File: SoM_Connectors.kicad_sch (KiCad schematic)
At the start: 5 parts, among them SW1 SW_DIP_x02

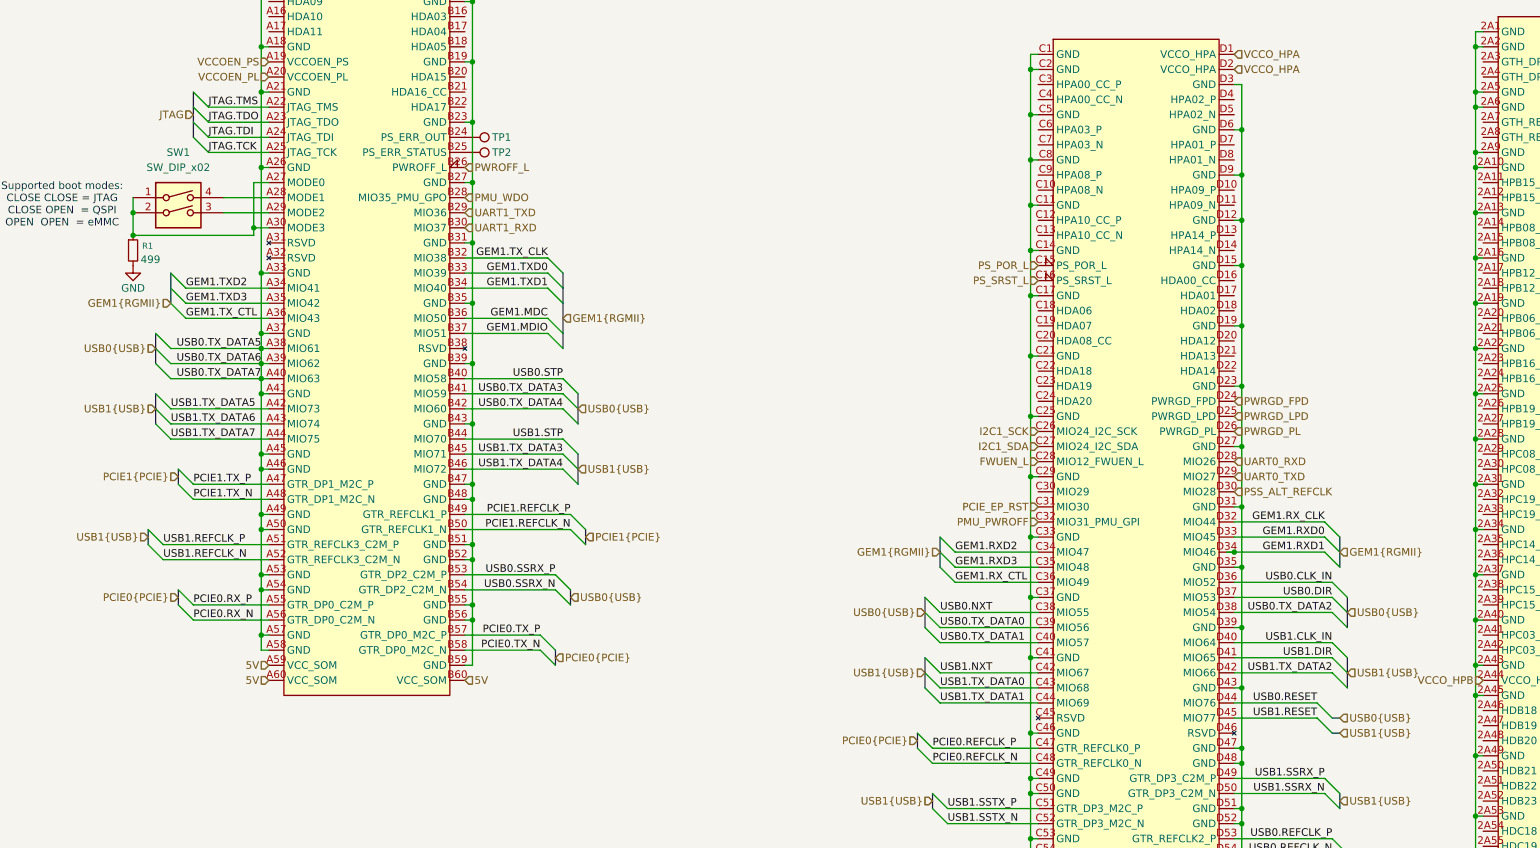
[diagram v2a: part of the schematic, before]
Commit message: MIO changes USB resets from 76/77 to shared 29 GEM1 MDIO moved from 50/51 to 76/77 I2C0 enabled on 50/51
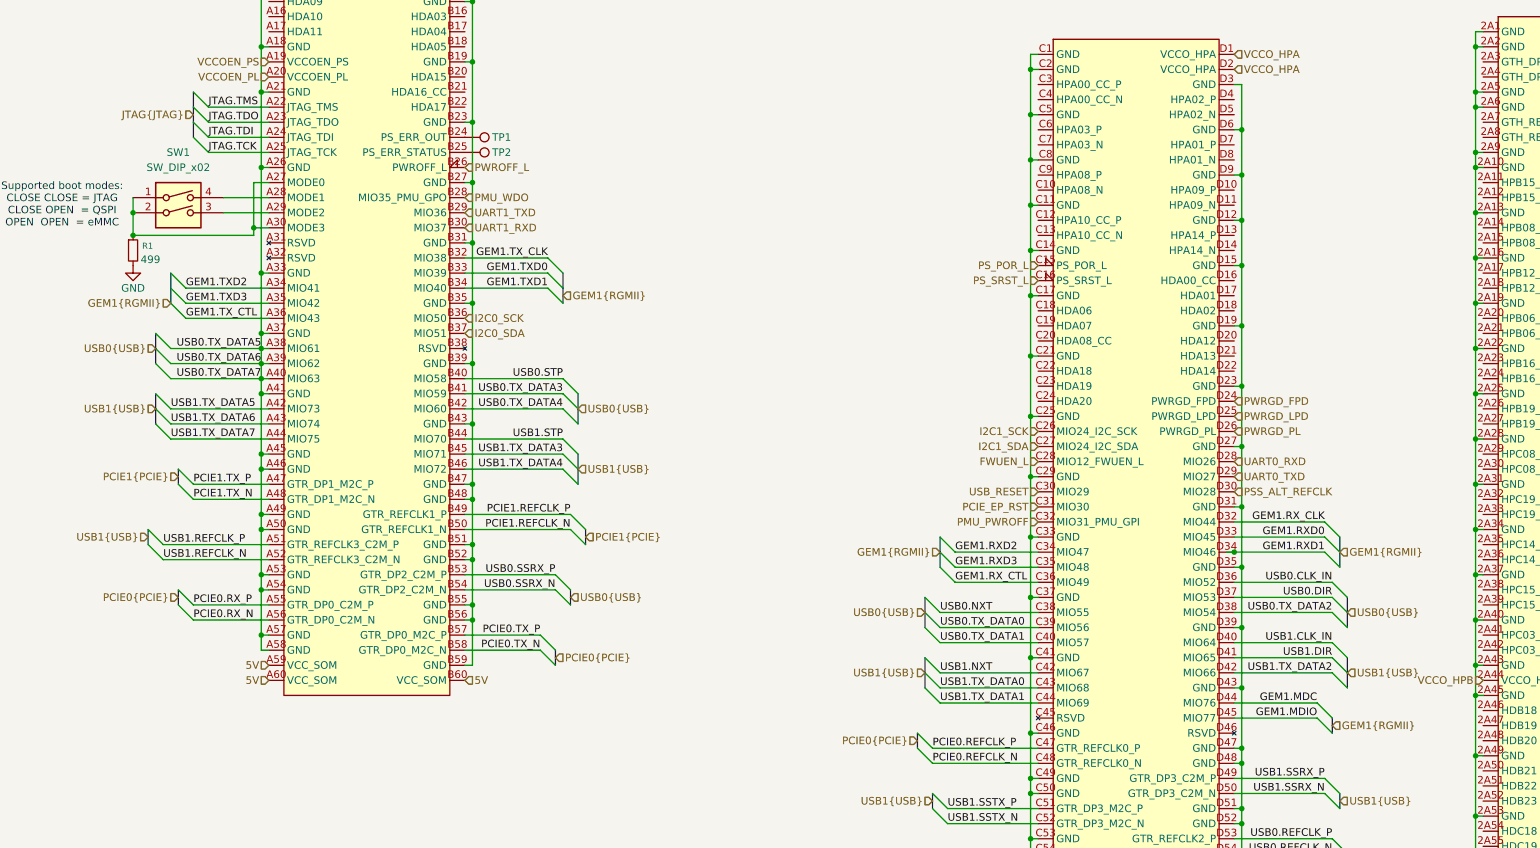
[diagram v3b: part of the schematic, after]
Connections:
- net USB0.RESET is gone; now on net GEM1.MDC: U1.D44 (MIO76)
- net USB1.RESET is gone; now on net GEM1.MDIO: U1.D45 (MIO77)
- net GEM1.MDC: no longer U1.B36 (MIO50)
- net GEM1.MDIO: no longer U1.B37 (MIO51)
- net USB_RESET: now reaches U1.C30 (MIO29)
- new net I2C0_SCK: U1.B36 (MIO50)
- new net I2C0_SDA: U1.B37 (MIO51)
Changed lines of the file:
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@@
 	)
 	(bus_entry
-		(at 105.41 185.42)
+		(at 236.22 196.85)
 		(size 2.54 2.54)
 		(stroke
@@
 	)
 	(bus_entry
-		(at 172.72 194.31)
-		(size -2.54 -2.54)
+		(at 105.41 185.42)
+		(size 2.54 2.54)
 		(stroke
 			(width 0)
@@
 	)
 	(bus_entry
-		(at 49.53 93.98)
+		(at 172.72 194.31)
 		(size -2.54 -2.54)
 		(stroke
@@
 	)
 	(bus_entry
-		(at 236.22 194.31)
-		(size 2.54 2.54)
+		(at 49.53 93.98)
+		(size -2.54 -2.54)
 		(stroke
 			(width 0)
@@
 	)
 	(bus_entry
-		(at 106.68 132.08)
-		(size 2.54 2.54)
-		(stroke
-			(width 0)
-			(type default)
-		)
-	)
-	(bus_entry
 		(at 107.95 172.72)
 		(size 2.54 2.54)
@@
 	)
 	(bus_entry
-		(at 106.68 129.54)
-		(size 2.54 2.54)
-		(stroke
-			(width 0)
-			(type default)
-		)
-	)
-	(bus_entry
-		(at 236.22 196.85)
+		(at 236.22 194.31)
 		(size 2.54 2.54)
 		(stroke
@@
 		)
 	)
-	(wire
-		(pts
-			(xy 106.68 132.08) (xy 92.71 132.08)
-		)
-		(stroke
-			(width 0)
-			(type default)
-		)
-	)
 	(bus
 		(pts
@@
 		)
 	)
+	(bus
+		(pts
+			(xy 238.76 196.85) (xy 238.76 199.39)
+		)
+		(stroke
+			(width 0)
+			(type default)
+		)
+	)
 	(wire
 		(pts
@@
 		)
 	)
-	(wire
-		(pts
-			(xy 106.68 129.54) (xy 92.71 129.54)
-		)
-		(stroke
-			(width 0)
-			(type default)
-		)
-	)
 	(bus
 		(pts
@@
 	(wire
 		(pts
-			(xy 236.22 194.31) (xy 222.25 194.31)
-		)
-		(stroke
-			(width 0)
-			(type default)
-		)
-	)
-	(wire
-		(pts
 			(xy 297.18 99.06) (xy 298.45 99.06)
 		)
@@
 	(wire
 		(pts
+			(xy 236.22 196.85) (xy 222.25 196.85)
+		)
+		(stroke
+			(width 0)
+			(type default)
+		)
+	)
+	(wire
+		(pts
 			(xy 262.89 142.24) (xy 264.16 142.24)
 		)
@@
 		)
 	)
-	(bus
-		(pts
-			(xy 109.22 132.08) (xy 109.22 134.62)
-		)
-		(stroke
-			(width 0)
-			(type default)
-		)
-	)
 	(wire
 		(pts
@@
 		)
 	)
-	(bus
-		(pts
-			(xy 109.22 127) (xy 109.22 132.08)
-		)
-		(stroke
-			(width 0)
-			(type default)
-		)
-	)
 	(wire
 		(pts
@@
 	(wire
 		(pts
-			(xy 236.22 196.85) (xy 222.25 196.85)
-		)
-		(stroke
-			(width 0)
-			(type default)
-		)
-	)
-	(wire
-		(pts
 			(xy 325.12 101.6) (xy 325.12 104.14)
 		)
@@
 		)
 	)
-	(bus
-		(pts
-			(xy 238.76 199.39) (xy 240.03 199.39)
-		)
-		(stroke
-			(width 0)
-			(type default)
-		)
-	)
 	(wire
 		(pts
@@
 		)
 	)
+	(wire
+		(pts
+			(xy 236.22 194.31) (xy 222.25 194.31)
+		)
+		(stroke
+			(width 0)
+			(type default)
+		)
+	)
 	(bus
 		(pts
@@
 		)
 	)
-	(bus
-		(pts
-			(xy 238.76 196.85) (xy 240.03 196.85)
-		)
-		(stroke
-			(width 0)
-			(type default)
-		)
-	)
 	(wire
 		(pts
@@
 		)
 	)
-	(label "USB1.SSRX_N"
-		(at 237.49 209.55 180)
+	(label "GEM1.MDC"
+		(at 236.22 194.31 180)
 		(effects
 			(font
@@
 		)
 	)
-	(label "USB1.RESET"
-		(at 236.22 196.85 180)
+	(label "USB1.SSRX_N"
+		(at 237.49 209.55 180)
 		(effects
 			(font
@@
 		)
 	)
-	(label "USB0.RESET"
-		(at 236.22 194.31 180)
-		(effects
-			(font
-				(size 1.27 1.27)
-			)
-			(justify right bottom)
-		)
-	)
 	(label "USB0.TX_DATA7"
 		(at 58.42 139.7 180)
@@
 		)
 	)
+	(label "GEM1.MDIO"
+		(at 236.22 196.85 180)
+		(effects
+			(font
+				(size 1.27 1.27)
+			)
+			(justify right bottom)
+		)
+	)
 	(label "USB0.REFCLK_N"
 		(at 238.76 219.71 180)
@@
 		)
 	)
-	(label "GEM1.MDC"
-		(at 106.68 129.54 180)
-		(effects
-			(font
-				(size 1.27 1.27)
-			)
-			(justify right bottom)
-		)
-	)
 	(label "GEM1.TXD2"
 		(at 45.72 124.46 0)
@@
 		)
 	)
-	(label "GEM1.MDIO"
-		(at 106.68 132.08 180)
-		(effects
-			(font
-				(size 1.27 1.27)
-			)
-			(justify right bottom)
-		)
-	)
 	(label "JTAG.TMS"
 		(at 49.53 93.98 0)
@@
 		)
 	)
-	(hierarchical_label "USB0{USB}"
-		(shape input)
-		(at 240.03 196.85 0)
-		(effects
-			(font
-				(size 1.27 1.27)
-			)
-			(justify left)
-		)
-	)
 	(hierarchical_label "USB1{USB}"
 		(shape input)
@@
 	(hierarchical_label "GEM1{RGMII}"
 		(shape input)
-		(at 109.22 129.54 0)
+		(at 109.22 125.73 0)
 		(effects
 			(font
@@
 		)
 	)
-	(hierarchical_label "JTAG"
+	(hierarchical_label "JTAG{JTAG}"
 		(shape input)
 		(at 46.99 95.25 180)
@@
 		)
 	)
+	(hierarchical_label "USB_RESET"
+		(shape input)
+		(at 189.23 158.75 180)
+		(effects
+			(font
+				(size 1.27 1.27)
+			)
+			(justify right)
+		)
+	)
 	(hierarchical_label "USB0{USB}"
 		(shape input)
@@
 		)
 	)
+	(hierarchical_label "GEM1{RGMII}"
+		(shape input)
+		(at 238.76 198.12 0)
+		(effects
+			(font
+				(size 1.27 1.27)
+			)
+			(justify left)
+		)
+	)
 	(hierarchical_label "VCCO_HPA"
 		(shape input)
@@
 		)
 	)
-	(hierarchical_label "PMU_PWROFF"
+	(hierarchical_label "I2C0_SCK"
 		(shape input)
-		(at 189.23 163.83 180)
+		(at 92.71 129.54 0)
 		(effects
 			(font
 				(size 1.27 1.27)
 			)
-			(justify right)
+			(justify left)
 		)
 	)
-	(hierarchical_label "5V"
+	(hierarchical_label "I2C0_SDA"
 		(shape input)
-		(at 92.71 190.5 0)
+		(at 92.71 132.08 0)
 		(effects
 			(font
@@
 		)
 	)
-	(hierarchical_label "USB1{USB}"
+	(hierarchical_label "PMU_PWROFF"
 		(shape input)
-		(at 241.3 189.23 0)
+		(at 189.23 163.83 180)
+		(effects
+			(font
+				(size 1.27 1.27)
+			)
+			(justify right)
+		)
+	)
+	(hierarchical_label "5V"
+		(shape input)
+		(at 92.71 190.5 0)
 		(effects
 			(font
@@
 	(hierarchical_label "USB1{USB}"
 		(shape input)
-		(at 240.03 199.39 0)
+		(at 241.3 189.23 0)
 		(effects
 			(font

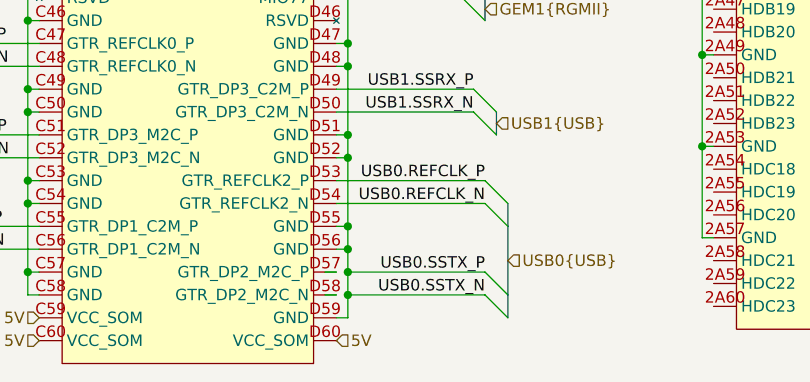
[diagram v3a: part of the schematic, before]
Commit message: fixed USB0.SSTX connections fixed JTAG bus label adjust hier pins in top schematic fixed USB4750 footprint shield pins names
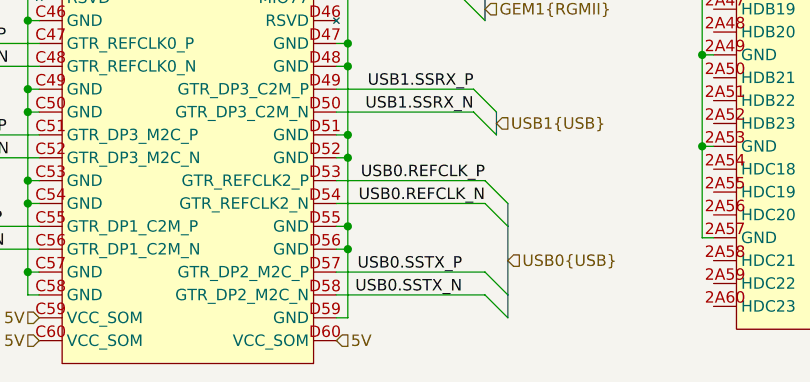
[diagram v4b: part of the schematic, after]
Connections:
- net USB0.SSTX_N: now also U1.D58 (GTR_DP2_M2C_N); no longer U1.D12 (GND), U1.D15 (GND), U1.D19 (GND), U1.D23 (GND), U1.D27 (GND), U1.D3 (GND), U1.D31 (GND), U1.D35 (GND), U1.D39 (GND), U1.D43 (GND), U1.D47 (GND), U1.D48 (GND), U1.D51 (GND), U1.D52 (GND), U1.D55 (GND), U1.D56 (GND), U1.D59 (GND), U1.D6 (GND), U1.D9 (GND)
- net USB0.SSTX_P: now reaches U1.D57 (GTR_DP2_M2C_P)
- new net: U1.D12 (GND), U1.D15 (GND), U1.D19 (GND), U1.D23 (GND), U1.D27 (GND), U1.D3 (GND), U1.D31 (GND), U1.D35 (GND), U1.D39 (GND), U1.D43 (GND), U1.D47 (GND), U1.D48 (GND), U1.D51 (GND), U1.D52 (GND), U1.D55 (GND), U1.D56 (GND), U1.D59 (GND), U1.D6 (GND), U1.D9 (GND)
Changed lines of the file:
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@@
 	)
 	(junction
-		(at 223.52 229.87)
-		(diameter 0)
-		(color 0 0 0 0)
-	)
-	(junction
 		(at 360.68 152.4)
 		(diameter 0)
@@
 	)
 	(junction
-		(at 223.52 227.33)
-		(diameter 0)
-		(color 0 0 0 0)
-	)
-	(junction
 		(at 360.68 167.64)
 		(diameter 0)
@@
 	(wire
 		(pts
-			(xy 223.52 224.79) (xy 223.52 227.33)
-		)
-		(stroke
-			(width 0)
-			(type default)
-		)
-	)
-	(wire
-		(pts
 			(xy 298.45 88.9) (xy 298.45 96.52)
 		)
@@
 	(wire
 		(pts
-			(xy 223.52 229.87) (xy 223.52 232.41)
-		)
-		(stroke
-			(width 0)
-			(type default)
-		)
-	)
-	(wire
-		(pts
 			(xy 297.18 198.12) (xy 298.45 198.12)
 		)
@@
 	(wire
 		(pts
-			(xy 238.76 229.87) (xy 223.52 229.87)
+			(xy 222.25 229.87) (xy 238.76 229.87)
 		)
 		(stroke
@@
 	(bus
 		(pts
-			(xy 241.3 222.25) (xy 241.3 229.87)
-		)
-		(stroke
-			(width 0)
-			(type default)
-		)
-	)
-	(bus
-		(pts
 			(xy 44.45 154.94) (xy 44.45 157.48)
 		)
@@
 	(wire
 		(pts
-			(xy 220.98 229.87) (xy 222.25 229.87)
-		)
-		(stroke
-			(width 0)
-			(type default)
-		)
-	)
-	(wire
-		(pts
 			(xy 187.96 166.37) (xy 187.96 176.53)
 		)
@@
 		)
 	)
+	(bus
+		(pts
+			(xy 241.3 222.25) (xy 241.3 229.87)
+		)
+		(stroke
+			(width 0)
+			(type default)
+		)
+	)
 	(wire
 		(pts
@@
 	(wire
 		(pts
-			(xy 220.98 227.33) (xy 222.25 227.33)
-		)
-		(stroke
-			(width 0)
-			(type default)
-		)
-	)
-	(wire
-		(pts
 			(xy 92.71 76.2) (xy 93.98 76.2)
 		)
@@
 	(wire
 		(pts
-			(xy 238.76 227.33) (xy 223.52 227.33)
+			(xy 222.25 227.33) (xy 238.76 227.33)
 		)
 		(stroke
@@
 	(wire
 		(pts
-			(xy 223.52 227.33) (xy 223.52 229.87)
+			(xy 223.52 224.79) (xy 223.52 232.41)
 		)
 		(stroke
@@
 	)
 	(label "USB0.SSTX_N"
-		(at 238.76 229.87 180)
+		(at 236.22 229.87 180)
 		(effects
 			(font
@@
 	)
 	(label "USB0.SSTX_P"
-		(at 238.76 227.33 180)
+		(at 236.22 227.33 180)
 		(effects
 			(font
